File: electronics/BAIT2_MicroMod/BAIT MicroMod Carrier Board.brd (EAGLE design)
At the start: 95.2 x 96.5 mm, 110 parts, among them J1 microSD, J4 JST_6_PIN_VERTICAL, J5 QWIIC_RIGHT_ANGLE, U3 3.3V, U4 3.3V, U5 BQ27441-G1, X1 2.1mm DC, X2 BQ24074

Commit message: Board layout updates
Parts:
- removed ANT1: DIP SMA-K, Connector-new:SMA5P-SMD-5.1-6.5X6.5X16.5MM
- removed R16: DNP, Discrete-new:R0402
- moved R15 147.8 mm to (79.9, 78.2), turned to 90 degrees
- moved R14 147.5 mm to (82.0, 74.3), turned to 90 degrees
- moved TP2 139.2 mm to (69.8, 58.4)
- moved C12 138.2 mm to (80.0, 74.9)
- moved C11 135.1 mm to (80.0, 73.7)
- moved C10 132.0 mm to (72.4, 57.1), turned to 90 degrees
- moved ANT2 25.9 mm to (83.8, 78.7)
- moved LORA-E5 14.0 mm to (77.5, 64.8), turned to 90 degrees
- moved D_ASC 8.89 mm to (78.7, 47.0)
- moved D_RSSI\ 8.89 mm to (74.9, 47.0)
- moved D_RX 8.89 mm to (71.1, 47.0)
- moved D_TX 8.89 mm to (67.3, 47.0)
- moved E5_SWO 8.89 mm to (61.0, 63.5)
- moved MM_SWO 8.89 mm to (48.3, 50.8)
- moved R_ASC 8.89 mm to (78.7, 50.8)
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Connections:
- removed net N$10: ANT2.D, R16.2
- removed net N$13: ANT1.ANT, R15.2
- new net N$7: ANT2.D, R15.2
- net GND: no longer ANT1.GND1, ANT1.GND2, ANT1.GND3, ANT1.GND4
- net N$28: no longer R16.1
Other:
- board size 95.2 x 96.5 mm -> 95.2 x 94 mm
- board text added: "LiPo"

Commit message: Files for First Prototype production
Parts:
- removed 3V3_LED2: (no value), SparkFun-Jumpers:SMT-JUMPER_2_NC_TRACE_SILK
- removed BATT2: JST 2PH, adafruit:JST-PH-2-SMT-RA
- removed BT3: ML414H, SparkFun-Batteries:ML414H_IV01E
- removed D_ASC, D_RSSI\, D_RX: GREEN, SparkFun-LED:LED-0603
- removed D_TX: RED, SparkFun-LED:LED-0603
- removed LORA-E5: LoRa-E5-HF, moudle-new:MOUDLE28P-1.25-12X12X2.5MM
- removed MICROMOD: MICROMOD-2222-C, SparkFun-MicroMod:M.2-CONNECTOR-E
- removed REG1: S-1172B33-E6T1U, Ablic:HSOP-6_FH006-A-P-SD-2.1_ABL
- removed R_ASC: 4.7k, SparkFun-Resistors:0603
- removed R_RSSI, R_RX, R_TX: 1k, SparkFun-Resistors:0603
- removed S1: Reset, SparkFun-Switches:TACTILE_SWITCH_SMD_5.2MM
- removed S2: BOOT, SparkFun-Switches:TACTILE_SWITCH_SMD_5.2MM
- removed SOLAR_JST1: (no value), SparkFun-Connectors:JST-2-SMD
- removed U$23: (no value), microbuilder:ADAFRUIT_5MM
- removed USBC: (no value), SparkFun-Connectors:USB-C-16P-2LAYER-PADS
- removed X1: 2.1mm DC, microbuilder:DCJACK_2MM_SMT
- removed X2: BQ24074, adafruit_power:QFN16_3MM
- removed XBEE: XBEE, adafruit:XBEE
- added 3V3_LED, GND_CON: (no value), SparkFun-Jumpers:SMT-JUMPER_2_NC_TRACE_SILK
- added ANT1: 0868AT43A0020EANT_0868AT43A0020E_JOT, 2023-01-04_20-35-52_Library:ANT_0868AT43A0020E_JOT
- added BT1: ML414H, SparkFun-Batteries:ML414H_IV01E
- added C1, C17, C19, C20, C21, C23, C31, C8: 2.2uF, SparkFun-Capacitors:0603-POLAR
- added C16, C2, C24, C9: 0.1uF, SparkFun-Capacitors:EIA3216
- added C18: 0.15uF, SparkFun-Capacitors:EIA3216
- added C32, C34, C35, C37, C38: 100nf, OPL_Capacitor:C0603
- added C33: 4.7uF, Discrete-new:C0603
- added C36: 10uf, OPL_Capacitor:AVX-A
- added C39: 220pF, Capacitor:CAPC1608X85
- added D2, D3, D4: GREEN, SparkFun-LED:LED-0603
- added D5: RED, SparkFun-LED:LED-0603
- added F1: 6V/2A, Circuit-Protection:FUSC3215X82N
- added FB1: 600Ω/1.8A, SparkFun-Coils:0603
- added J10: QWIIC_RIGHT_ANGLE, SM04B-SRSS-TB_LF__SN_:JST_SM04B-SRSS-TB(LF)(SN)
- added J15: SM06B-SRSS-TB(LF)(SN), SM06B-SRSS-TB_LF__SN_:JST_SM06B-SRSS-TB(LF)(SN)
- added J2: ST-TF-003A, ST-TF-003A:SUNTECH_ST-TF-003A
- added J3: (no value), SparkFun-RF:XBEE-SMD
- added J6: JST 2PH, adafruit:JST-PH-2-SMT-RA
- added J7: MICROMOD-2222-C, SparkFun-MicroMod:M.2-CONNECTOR-E
- added J8: (no value), SparkFun-Connectors:JST-2-SMD
- added J9: (no value), SparkFun-Connectors:USB-C-16P-2LAYER-PADS
- added LINEIN, LINEOUT: (no value), SparkFun-Connectors:1X03
- added MIC_3V3, MIC_GND: (no value), SparkFun-Jumpers:SMT-JUMPER_3_2-NC_TRACE_SILK
- added MK1: ICS-43432, Audio-Devices:ICS-43432
- added MK1_LR: MK1_LR, SparkFun-Jumpers:SMT-JUMPER_3_1-NC_TRACE_SILK
- added MK2: SPH0645LM4H-B, SPH0645LM4H-B:MIC_SPH0645LM4H-B
- added MK2_LR: MK2_LR, SparkFun-Jumpers:SMT-JUMPER_3_1-NC_TRACE_SILK
- added R11, R5: 4.7K, OPL_Resistor:R0603
- added R18: 100K, OPL_Resistor:R0603
- added R2: 2.2K, OPL_Resistor:R0603
- added R4: 0R, OPL_Resistor:R0603
- added R6, R7, R8: 1K 1/10W, OPL_Resistor:R0603
- added SW1, SW2: SKQGADE010, OPL_Switch:SW4-SMD-5.2X5.2X1.5MM
- added TP1, TP3: PTR1TP06R, testpad:TP06R
- added U1: SGTL5000-32, Freescale:QFN-32-5MM
- added U10: TSL25911, 2023-02-07_20-42-29_Library:SON-06-FN_2000X2400_AMS
- added U2: AP7313, 2022-08-05_10-01-44_Library:SOT-23_DIO
- added U6: BQ24074, adafruit_power:QFN16_3MM
- added U7: LoRa-E5-HF, moudle-new:MOUDLE28P-1.25-12X12X2.5MM
- added U8: S-1172B33-E6T1U, Ablic:HSOP-6_FH006-A-P-SD-2.1_ABL
- added U9: BOSCH_TOOLS_BME680BOSCH_TOOLS_BME680_0_0, Bosch Tools - BME680:BOSCH_TOOLS_BME680_0
- C10: value 4.7uF -> 4.7uf; device Discrete-new:C0603 -> OPL_Capacitor:C0603
- C13, C14, C28: value 1.0uF -> 1uf; device SparkFun-Capacitors:0603 -> OPL_Capacitor:C0603
- C15, C22, C4, C5: value 10uF -> 4.7uf; device microbuilder:0805-NO -> OPL_Capacitor:C0603
- C25, C30: value 0.22uF -> 220nf; device SparkFun-Capacitors:0603 -> OPL_Capacitor:C0603
- C26, C29, C6: value 0.1uF -> 100nf; device SparkFun-Capacitors:0603 -> OPL_Capacitor:C0603
- C27: value 10uF -> 10uf; device SparkFun-Capacitors:EIA3216 -> OPL_Capacitor:AVX-A
- C3: value 1.0uF -> 1uf; device SparkFun-Capacitors:0603-CAP -> OPL_Capacitor:C0603
- D17, D21: device microbuilder:CHIPLED_0603 -> SparkFun-LED:LED-0603
- J1: value microSD -> SJ-43516-SMT; device SparkFun-Connectors:MICRO-SD-SOCKET -> SnapEDA-Library:CUI_SJ-43516-SMT
- R1: value 180 -> 200K; device SparkFun-Resistors:0603 -> OPL_Resistor:R0603
- R10: value 20k -> 20K; device SparkFun-Resistors:0603 -> OPL_Resistor:R0603
- R14, R15: device Discrete-new:R0402 -> OPL_Resistor:R0603
- R21, R3, R36: value 100k -> 100K; device SparkFun-Resistors:0603 -> OPL_Resistor:R0603
- R23: value 1k -> 1K 1/10W; device SparkFun-Resistors:0603 -> OPL_Resistor:R0603
- R24: value 4.7k -> 4.7K; device SparkFun-Resistors:0603 -> OPL_Resistor:R0603
- R32: value 3.3k -> 3.3K; device SparkFun-Resistors:0603 -> OPL_Resistor:R0603
- R34, R35: value 2.2k -> 2.2K; device SparkFun-Resistors:0603 -> OPL_Resistor:R0603
- R38, R41, R42, R43, R44: value 10K -> 10K 1/10W; device microbuilder:0603-NO -> OPL_Resistor:R0603
- R39: device microbuilder:0603-NO -> OPL_Resistor:R0603
- R40: value 1K -> 1K 1/10W; device microbuilder:0603-NO -> OPL_Resistor:R0603
- R9: value 10k -> 10K 1/10W; device SparkFun-Resistors:0603 -> OPL_Resistor:R0603
- TH1, TH2, TH3, TH4: device varistor:CT/CN0603 -> NTCG163JX103DT1S:THERM_NTCG163JX103DT1S
- moved POWER_PINS 93.0 mm to (81.3, 3.81)
- moved J4 86.3 mm to (14.6, 50.5), turned to 180 degrees
- moved R14 68.2 mm to (13.9, 71.8), turned to 270 degrees
- moved C12 67.5 mm to (12.6, 70.4)
- moved ANT2 67.3 mm to (16.5, 77.5), turned to 90 degrees
- moved C11 64.9 mm to (15.2, 70.3), turned to 180 degrees
- moved R15 64.3 mm to (15.7, 74.0)
- moved R34 55.8 mm to (36.8, 36.8), turned to 0 degrees
- moved C14 54.5 mm to (32.6, 30.5), turned to 180 degrees
- moved R21 54.5 mm to (34.3, 33.0), turned to 270 degrees
- moved J5 51.7 mm to (40.6, 41.9), turned to 270 degrees
- moved R35 51.3 mm to (39.1, 36.8), turned to 0 degrees
- moved U4 51.2 mm to (35.6, 30.5), turned to 90 degrees
- moved C13 49.7 mm to (42.4, 43.2), turned to 180 degrees
- moved QWIIC_PWR 48.4 mm to (43.2, 36.8)
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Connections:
- removed net GND1: SOLAR_JST1.1, X1.2, X1.3
- removed net OUT: X2.5
- removed net PA15/SDA: LORA-E5.6
- removed net PB15/SCL: LORA-E5.5
- removed net RX2: MICROMOD.20
- removed net THERM: TH1.1, TH3.1, THERM2.2, X2.1
- removed net TX2: MICROMOD.22
- removed net V+1: REG1.6
- removed net VCC: XBEE.1
- new net 3V3_B: C34.1, C35.1, J10.2, J15.1, MIC_3V3.2, MK1_LR.1, MK2_LR.3, TP1.TP, U10.5, U9.8
- new net 3V3_ICS: C37.1, MIC_3V3.3, MK1.3
- new net 3V3_SPH: C38.1, C39.1, MIC_3V3.1, MK2.5
- new net AGND: C18.-, GND_CON.1, LINEIN.1, LINEOUT.1, U1.1, U1.3, U1.7
- new net GND_B: C32.2, C34.2, C35.2, J10.1, J10.S1, J10.S2, J15.2, J15.S1, J15.S2, MIC_GND.2, MK1_LR.3, MK2_LR.1, R18.1, TP3.TP, U10.3, U9.1, U9.5, U9.7
- new net GND_ICS: C37.2, MIC_GND.3, MK1.2, MK1.4
- new net GND_SPH: C38.2, C39.2, MIC_GND.1, MK2.3
- new net INT_B: U10.2
- new net N$11: ANT1.1, R4.2
- new net N$13: C19.-, LINEOUT.3
- new net N$14: C20.-, LINEOUT.2
- new net N$15: C21.-, LINEIN.3
- new net N$17: C23.-, LINEIN.2
- new net N$18: C19.+, U1.11
- new net N$20: C20.+, U1.12
- new net N$21: C21.+, U1.13
- new net N$22: C23.+, U1.14
- new net N$33: C24.-, J1.1, R2.2
- new net N$35: J1.3, U1.2
- new net N$36: F1.1, J9.VBUS1, J9.VBUS2
- new net N$38: C18.+, U1.10
- new net N$39: C31.+, R2.1, U1.16
- new net N$40: C24.+, U1.15
- new net N$41: C8.+, U1.30, U2.2
- new net N$46: C1.+, C2.+, FB1.2, U1.5
- new net N$54: C32.1, R11.2, U9.6
- new net N$55: R11.1, U9.2
- new net N$8: J1.2, U1.6
- new net SCK_B: J15.3, MK1.6, MK2.4
- new net SCL_B: J10.4, U10.1, U9.4
- new net SDA_B: J10.3, U10.6, U9.3
- new net SD_B: J15.4, MK1.7, MK2.6, R18.2
- new net SEL_MK1: MK1.1, MK1_LR.2
- new net SEL_MK2: MK2.2, MK2_LR.2
- new net USB_VIN: D15.A, F1.2, J7.9
- new net WS_B: J15.5, MK1.5, MK2.1
- net !BOOT!: now also J7.11, SW2.2; no longer MICROMOD.11, S2.3, S2.4
- net !CE: now also U6.4; no longer X2.4
- net !CHG: now also U6.9; no longer X2.9
- net !PGOOD: now also U6.7; no longer X2.7
- net !RESET!: now also J7.6, SW1.2; no longer MICROMOD.6, S1.3, S1.4
- net 3.3V: now also 3V3_LED.2, C16.+, C17.+, C33.2, C36.+, C9.+, FB1.1, J3.1, J7.2, J7.74, J_RX.1, U1.20, U2.1, U7.1; no longer 3V3_LED2.2, J_RX.2, LORA-E5.1, MICROMOD.2, MICROMOD.74
- net 3.3V_EN: now also J7.4; no longer MICROMOD.4
- net 3.3V_LP: now also J2.4; no longer J1.VCC
- net A0: now also J7.34; no longer MICROMOD.34
- net A1: now also J7.38; no longer MICROMOD.38
- net ASC: now also J3.15; no longer XBEE.15
- net CLK/SCK: now also J2.5, JP_SCK.2; no longer J1.SCLK, JP_SCK.3
- net CMD/CIPO: now also J2.3, JP_CIPO.2; no longer J1.DI/CMD, JP_CIPO.3
- net D0: now also J7.10; no longer MICROMOD.10
- net D1: now also J7.18; no longer MICROMOD.18
- net DAT0/COPI: now also J2.7, JP_COPI.2; no longer J1.DO/DAT0, JP_COPI.3
- net DAT3/!CS!: now also J2.2, JP_CS.2; no longer J1.CS/DAT3, JP_CS.3
- net GND: now also BT1.-, C1.-, C16.-, C17.-, C2.-, C31.-, C33.1, C36.-, C8.-, C9.-, D2.C, D3.C, GND_CON.2, J2.6, J2.G1, J2.G2, J2.G3, J2.G4, J3.10, J6.2, J7.1, J7.33, J7.36, J7.39, J7.45, J7.7, J7.75, J8.1, J9.GND, J9.GND2, SW1.4, SW2.4, U1.31, U1.32, U1.PAD, U2.3, U6.14, U6.6, U6.8, U6.THERMAL, U7.14, U7.16, U7.2, U7.22, U8.2, U8.5; no longer BATT2.2, BT3.-, D_ASC.C, D_RSSI\.C, J1.CD1, J1.GND, J1.GND1, J1.GND3, LORA-E5.14, LORA-E5.16, LORA-E5.2, LORA-E5.22, MICROMOD.1, MICROMOD.33, MICROMOD.36, MICROMOD.39, MICROMOD.45, MICROMOD.7, MICROMOD.75, REG1.2, REG1.5, S1.1, S1.2, S2.1, S2.2, USBC.GND, USBC.GND2, X2.14, X2.6, X2.8, X2.THERMAL, XBEE.10
- net GPOUT: now also J7.71
- net HEADER_!CS!: now also J7.40; no longer MICROMOD.40
- net I2C_!INT!: now also J7.16; no longer MICROMOD.16
- net I2C_SCL: now also J7.14, U1.29; no longer MICROMOD.14
- net I2C_SDA: now also J7.12, U1.27; no longer MICROMOD.12
- net I2S_SCK: now also J7.50; no longer MICROMOD.50
- net I2S_SD: now also J7.54; no longer MICROMOD.54
- net I2S_WS: now also J7.52; no longer MICROMOD.52
- net ILIM: now also U6.12; no longer X2.12
- net ISET: now also U6.16; no longer X2.16
- net ITERM: now also U6.15; no longer X2.15
- net LR_SEL: now also J7.73; no longer MICROMOD.73
- net N$16: now also 3V3_LED.1; no longer 3V3_LED2.1
- net N$19: now also U7.28; no longer LORA-E5.28
- net N$23: now also BT1.+; no longer BT3.+
- net N$25: now also R5.2; no longer R_ASC.2
- net N$28: now also R4.1
- net N$3: now also J_RX.2, R7.2; no longer J_RX.1, R_RX.2
- net N$30: now also J8.2; no longer SOLAR_JST1.2, X1.1, X1.1'
- net N$34: now also D2.A, R5.1; no longer D_ASC.A, R_ASC.1
- net N$4: now also J9.A5; no longer USBC.A5
- net N$42: now also R6.2; no longer R_RSSI.2
- net N$43: now also D3.A, R6.1; no longer D_RSSI\.A, R_RSSI.1
- net N$44: now also R8.2; no longer R_TX.2
- net N$45: now also D5.A, R8.1; no longer D_TX.A, R_TX.1
- net N$48: now also J1.4, U1.4; no longer D15.A, USBC.VBUS1, USBC.VBUS2
- net N$5: now also J9.B5; no longer USBC.B5
- net N$6: now also U8.1; no longer REG1.1
- net N$9: now also D4.A, R7.1; no longer D_RX.A, R_RX.1
- net PA0/D0: now also U7.23; no longer LORA-E5.23
- net PA10/MOSI: now also U7.27; no longer LORA-E5.27
- net PA13/SWDIO: now also U7.3; no longer LORA-E5.3
- net PA14/SWCLK: now also U7.4; no longer LORA-E5.4
- net PA2/TX2: now also U7.19; no longer LORA-E5.19
- net PA3/RX2: now also E5_EXTRA_PINS.14, U7.18; no longer E5_EXTRA_PINS.12, LORA-E5.18
- net PA9/D9: now also E5_EXTRA_PINS.11, U7.21; no longer E5_EXTRA_PINS.15, LORA-E5.21
- net PB10/D10: now also E5_EXTRA_PINS.12, U7.20; no longer E5_EXTRA_PINS.14, LORA-E5.20
- net PB13/BOOT/SCK: now also U7.24; no longer LORA-E5.24
- net PB14/MISO: now also U7.26; no longer LORA-E5.26
- net PB3/A3: now also U7.8; no longer LORA-E5.8
- net PB4/A4: now also U7.7; no longer LORA-E5.7
- net PB5/LED: now also E5_EXTRA_PINS.10, U7.11; no longer E5_EXTRA_PINS.8, LORA-E5.11
- net PB9/NSS: now also U7.25; no longer LORA-E5.25
- net PC0/RX1: now also E5_EXTRA_PINS.8, U7.13; no longer E5_EXTRA_PINS.10, LORA-E5.13
- net PC1/TX1: now also U7.12; no longer LORA-E5.12
- net PERIPHERAL_PWR_CTRL: now also J7.42; no longer MICROMOD.42
- net PWM0: now also J7.32; no longer MICROMOD.32
- net PWM1: now also J7.47; no longer MICROMOD.47
- net QWIIC_PWR_CTRL: now also J7.44; no longer MICROMOD.44
- net RF: now also U7.15; no longer LORA-E5.15
- net RSSI: now also J3.6; no longer XBEE.6
- net RST: now also E5_EXTRA_PINS.15, U7.17; no longer E5_EXTRA_PINS.11, LORA-E5.17
- net RTC_3V: now also J7.72; no longer MICROMOD.72
- net RX: now also D4.C, J3.2, J7.19, U7.9; no longer D_RX.C, LORA-E5.9, MICROMOD.19, XBEE.2
- net SD_!CS!: now also J7.55; no longer MICROMOD.55
- net SD_CLK: now also J7.60, JP_SCK.3; no longer JP_SCK.2, MICROMOD.60
- net SD_CMD: now also J7.62, JP_CIPO.3; no longer JP_CIPO.2, MICROMOD.62
- net SD_DATA0: now also J7.64, JP_COPI.3; no longer JP_COPI.2, MICROMOD.64
- net SD_DATA1: now also J2.8, J7.66; no longer J1.DAT1, MICROMOD.66
- net SD_DATA2: now also J2.1, J7.68; no longer J1.DAT2, MICROMOD.68
- net SD_DATA3: now also J7.70, JP_CS.3; no longer JP_CS.2, MICROMOD.70
- net SPI_CIPO: now also J7.61; no longer MICROMOD.61
- net SPI_COPI: now also J7.59; no longer MICROMOD.59
- net SPI_SCK: now also J7.57; no longer MICROMOD.57
- net SWDCK: now also J7.21; no longer MICROMOD.21
- net SWDIO: now also J7.23; no longer MICROMOD.23
- net TS: now also TH1.1, TH3.1, THERM2.2, U6.1
- net TX: now also D5.C, J3.3, J7.17, U7.10; no longer D_TX.C, LORA-E5.10, MICROMOD.17, XBEE.3
- net USB_D+: now also J7.3, J9.A6, J9.B6; no longer MICROMOD.3, USBC.A6, USBC.B6
- net USB_D-: now also J7.5, J9.A7, J9.B7; no longer MICROMOD.5, USBC.A7, USBC.B7
- net V+: now also U6.10, U6.11, U6.5, U8.6; no longer X2.10, X2.11
- net VBUS: now also U6.13; no longer X2.13
- net VIN: now also J6.1; no longer BATT2.1, MICROMOD.9
- net VIN/3: now also J7.49; no longer MICROMOD.49
- net V_BATT: now also U6.2, U6.3; no longer X2.2, X2.3
- net XB_ON: now also J3.13; no longer XBEE.13
- net XB_RST: now also J3.5; no longer XBEE.5
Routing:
- net 3.3V: track 0.00 -> 271.8 mm, vias 0 -> 13
- net GND: track 7.68 -> 153.4 mm, vias 1 -> 17
- net V+: track 10.4 -> 109.5 mm, vias 1 -> 5
- net VBUS: track 13.9 -> 101.7 mm, vias 0 -> 3
- net !RESET!: track 0.00 -> 79.7 mm, vias 0 -> 2
- net TS: track 0.00 -> 74.5 mm, vias 0 -> 4
- net I2C_SCL: track 0.00 -> 74.4 mm, vias 0 -> 4
- net I2C_SDA: track 0.00 -> 74.1 mm, vias 0 -> 2
- net !BOOT!: track 0.00 -> 72.1 mm, vias 0 -> 2
- net USB_VIN: track 0.00 -> 69.8 mm, vias 0 -> 2
- net RF: track 0.00 -> 66.0 mm, vias 0 -> 2
- net RX: track 0.00 -> 66.0 mm, vias 0 -> 4
- net RST: track 0.00 -> 63.7 mm, vias 0 -> 3
- net USB_D+: track 0.00 -> 61.5 mm, vias 0 -> 6
- net TX: track 0.00 -> 61.0 mm, vias 0 -> 4
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- added copper zone on layer 1, net CUTOUT
- added copper zone on layer 1, net GND
- added copper zone on layer 16, net GND_B
- removed copper zone on layer 1, net OUT
- removed copper zone on layer 1, net VLIPO
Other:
- board size 95.2 x 94 mm -> 92.7 x 80 mm
- board text added: "50 ohm impedance control on the RF line from its origin on the WIO-E5 chip through to ANT1 and ANT2"
- board text added: "BAIT"
- board text added: "SmallThings"
- board text added: "V2.0.1 (23F14)"
- board text added: "by"
- board text removed: "0.5A"
- board text removed: "1.0A"
- board text removed: "1.5A"
- board text removed: "LiPo"
- board text removed: "LiPo Batt"
- board text removed: "Solar/DC In is 10V Max"
- board text removed: "Use any 3.7/4.2V LiPoly/LiIon"

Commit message: Schematic fix for faulty connection between Teensy and LORA-E5
Swapped RX and TX pins. Fixes #7
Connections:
- net RX: now also U7.10; no longer U7.9
- net TX: now also U7.9; no longer U7.10
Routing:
- net TX: track 61.0 -> 56.5 mm
- net RX: track 66.0 -> 61.8 mm
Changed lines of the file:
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@@
 <wire x1="42.4197125" y1="52.9932" x2="42.7665125" y2="53.34" width="0.2032" layer="1"/>
 <wire x1="42.7665125" y1="53.34" x2="45.157125" y2="53.34" width="0.2032" layer="1"/>
-<wire x1="62.25" y1="59.19631875" x2="62.25" y2="60.04" width="0.2032" layer="1"/>
-<wire x1="60.20368125" y1="57.15" x2="62.25" y2="59.19631875" width="0.2032" layer="1"/>
 <wire x1="45.157125" y1="53.34" x2="48.967125" y2="57.15" width="0.2032" layer="1"/>
 <wire x1="48.967125" y1="57.15" x2="51.816" y2="57.15" width="0.2032" layer="1"/>
@@
 <contactref element="J3" pad="3"/>
 <contactref element="J7" pad="17"/>
-<contactref element="U7" pad="10"/>
-<wire x1="62.25" y1="60.04" x2="62.25" y2="58.44" width="0.2032" layer="1"/>
 <wire x1="62.25" y1="58.44" x2="62.23" y2="58.42" width="0.2032" layer="1"/>
 <via x="62.23" y="58.42" extent="1-16" drill="0.35"/>
@@
 <wire x1="62.23" y1="49.53" x2="61.353" y2="48.653" width="0.2032" layer="1"/>
 <wire x1="61.353" y1="48.653" x2="61.353" y2="48.26" width="0.2032" layer="1"/>
+<contactref element="U7" pad="9"/>
+<wire x1="61" y1="59.19631875" x2="61" y2="60.04" width="0.2032" layer="1"/>
+<wire x1="62.23" y1="58.42" x2="61" y2="59.19631875" width="0" layer="19" extent="1-1"/>
+<wire x1="60.20368125" y1="57.15" x2="61" y2="59.19631875" width="0" layer="19" extent="1-1"/>
 </signal>
 <signal name="RX" class="2">
@@
 <wire x1="42.2724125" y1="53.3488" x2="42.7636125" y2="53.84" width="0.2032" layer="1"/>
 <wire x1="42.7636125" y1="53.84" x2="44.95" y2="53.84" width="0.2032" layer="1"/>
-<wire x1="61" y1="59.19631875" x2="61" y2="60.04" width="0.2032" layer="1"/>
 <wire x1="44.95" y1="53.84" x2="48.76000625" y2="57.65000625" width="0.2032" layer="1"/>
 <wire x1="48.76000625" y1="57.65000625" x2="52.705" y2="57.65000625" width="0.2032" layer="1"/>
 <wire x1="52.705" y1="57.65000625" x2="59.4536875" y2="57.65000625" width="0.2032" layer="1"/>
-<wire x1="59.4536875" y1="57.65000625" x2="61" y2="59.19631875" width="0.2032" layer="1"/>
 <via x="53.9402" y="73.66" extent="1-16" drill="0.35"/>
 <wire x1="53.9402" y1="73.66" x2="52.7737" y2="72.4935" width="0.2032" layer="16"/>
@@
 <contactref element="J3" pad="2"/>
 <contactref element="J7" pad="19"/>
-<contactref element="U7" pad="9"/>
 <wire x1="65.163" y1="48.26" x2="64.77" y2="48.653" width="0.2032" layer="1"/>
 <wire x1="64.77" y1="48.653" x2="64.77" y2="49.53" width="0.2032" layer="1"/>
@@
 <wire x1="62.865" y1="51.435" x2="62.865" y2="61.6698" width="0.2032" layer="16"/>
 <via x="62.865" y="61.6698" extent="1-16" drill="0.35"/>
-<wire x1="61.546" y1="61.2952125" x2="61.546" y2="60.586" width="0.2032" layer="1"/>
-<wire x1="61.546" y1="60.586" x2="61" y2="60.04" width="0.2032" layer="1"/>
 <wire x1="62.865" y1="61.6698" x2="61.9205875" y2="61.6698" width="0.2032" layer="1"/>
-<wire x1="61.9205875" y1="61.6698" x2="61.546" y2="61.2952125" width="0.2032" layer="1"/>
 <wire x1="53.9402" y1="73.66" x2="54" y2="73.7198" width="0.2032" layer="1"/>
 <wire x1="54" y1="73.7198" x2="54" y2="75.15" width="0.2032" layer="1"/>
+<contactref element="U7" pad="10"/>
+<wire x1="62.25" y1="59.19631875" x2="62.25" y2="60.04" width="0.2032" layer="1"/>
+<wire x1="61.9205875" y1="61.6698" x2="62.25" y2="60.04" width="0" layer="19" extent="1-1"/>
+<wire x1="59.4536875" y1="57.65000625" x2="62.25" y2="59.19631875" width="0" layer="19" extent="1-1"/>
 </signal>
 <signal name="RTC_3V" class="1">

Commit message: Connect SGTL to I2S2 pins on micromod connector
Solves #6 in schematic, but creates #14
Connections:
- removed net D0: J7.10, MICROMOD_EXTRA_PINS.4
- removed net D1: J7.18, MICROMOD_EXTRA_PINS.3
- removed net PWM0: J7.32, R1.1
- removed net PWM1: J7.47, MICROMOD_EXTRA_PINS.5
- new net I2S2_MCLK: J7.63, U1.21
- new net I2S2_RX: J7.18, U1.25
- new net I2S2_SCK: J7.10, U1.24
- new net I2S2_TX: J7.47, U1.26
- new net I2S2_WS: J7.32, U1.23
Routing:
- net D0: track 48.3 -> 0.00 mm
- net D1: track 47.3 -> 0.00 mm
- net PWM1: track 46.7 -> 0.00 mm
- net PWM0: track 43.9 -> 0.00 mm, vias 4 -> 0
- net I2S2_WS: track 0.00 -> 42.1 mm, vias 0 -> 4
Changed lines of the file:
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@@
 <wire x1="4.826" y1="65.405" x2="1.778" y2="62.357" width="0.2032" layer="16"/>
 </signal>
-<signal name="PWM0">
-<contactref element="R1" pad="1"/>
+<signal name="I2S2_WS">
 <wire x1="33.25" y1="56.885" x2="33.25" y2="55.6302" width="0.2032" layer="1"/>
 <via x="33.25" y="55.6302" extent="1-16" drill="0.35"/>
@@
 <wire x1="52.2078" y1="38.0891625" x2="58.48348125" y2="31.81348125" width="0.2032" layer="16"/>
 <via x="58.48348125" y="31.81348125" extent="1-16" drill="0.35"/>
-<wire x1="58.48348125" y1="31.81348125" x2="58.48348125" y2="30.12348125" width="0.2032" layer="1"/>
-<wire x1="58.48348125" y1="30.12348125" x2="58.42" y2="29.972" width="0.2032" layer="1"/>
 <contactref element="J7" pad="32"/>
-</signal>
-<signal name="PWM1">
-<contactref element="MICROMOD_EXTRA_PINS" pad="5"/>
-<contactref element="J7" pad="47"/>
-<wire x1="12.7" y1="46.99" x2="27.94" y2="46.99" width="0.2032" layer="1"/>
-<wire x1="28.43808125" y1="45.66969375" x2="28.77865625" y2="45.32911875" width="0.2032" layer="1"/>
-<wire x1="28.77865625" y1="45.32911875" x2="29.26030625" y2="45.32911875" width="0.2032" layer="1"/>
-<wire x1="29.26030625" y1="45.32911875" x2="29.60088125" y2="45.66969375" width="0.2032" layer="1"/>
-<wire x1="29.60088125" y1="45.66969375" x2="29.60088125" y2="46.15134375" width="0.2032" layer="1"/>
-<wire x1="29.60088125" y1="46.15134375" x2="29.5" y2="46.252225" width="0.2032" layer="1"/>
-<wire x1="29.5" y1="46.252225" x2="29.5" y2="49.335" width="0.2032" layer="1"/>
-<wire x1="27.94" y1="46.99" x2="28.43808125" y2="46.49191875" width="0.2032" layer="1"/>
-<wire x1="28.43808125" y1="46.49191875" x2="28.43808125" y2="45.66969375" width="0.2032" layer="1"/>
-<wire x1="0.5842" y1="49.16250625" x2="1.28350625" y2="48.4632" width="0.2032" layer="1"/>
-<wire x1="1.28350625" y1="48.4632" x2="2.27249375" y2="48.4632" width="0.2032" layer="1"/>
-<wire x1="1.778" y1="59.817" x2="1.778" y2="58.96529375" width="0.2032" layer="1"/>
-<wire x1="1.778" y1="58.96529375" x2="0.5842" y2="57.77149375" width="0.2032" layer="1"/>
-<wire x1="2.97829375" y1="49.169" x2="10.521" y2="49.169" width="0.2032" layer="1"/>
-<wire x1="10.521" y1="49.169" x2="12.7" y2="46.99" width="0.2032" layer="1"/>
-<wire x1="2.27249375" y1="48.4632" x2="2.97829375" y2="49.169" width="0.2032" layer="1"/>
-<wire x1="0.5842" y1="57.77149375" x2="0.5842" y2="49.16250625" width="0.2032" layer="1"/>
-</signal>
-<signal name="D0">
-<contactref element="MICROMOD_EXTRA_PINS" pad="4"/>
-<wire x1="38.75" y1="56.885" x2="38.75" y2="58.1398" width="0.2032" layer="1"/>
-<contactref element="J7" pad="10"/>
-<wire x1="38.75" y1="58.1398" x2="30.04518125" y2="66.84461875" width="0.2032" layer="1"/>
-<wire x1="30.04518125" y1="66.84461875" x2="7.15461875" y2="66.84461875" width="0.2032" layer="1"/>
-<wire x1="7.15461875" y1="66.84461875" x2="3.81" y2="63.5" width="0.2032" layer="1"/>
-<wire x1="3.81" y1="63.5" x2="3.81" y2="59.309" width="0.2032" layer="1"/>
-<wire x1="3.81" y1="59.309" x2="1.778" y2="57.277" width="0.2032" layer="1"/>
-</signal>
-<signal name="D1">
-<contactref element="MICROMOD_EXTRA_PINS" pad="3"/>
-<contactref element="J7" pad="18"/>
-<wire x1="4.445" y1="57.404" x2="1.778" y2="54.737" width="0.2032" layer="1"/>
-<wire x1="36.75" y1="56.885" x2="36.654" y2="56.981" width="0.2032" layer="1"/>
-<wire x1="36.654" y1="56.981" x2="36.654" y2="58.058025" width="0.2032" layer="1"/>
-<wire x1="36.654" y1="58.058025" x2="28.672025" y2="66.04" width="0.2032" layer="1"/>
-<wire x1="4.445" y1="62.865" x2="4.445" y2="57.404" width="0.2032" layer="1"/>
-<wire x1="28.672025" y1="66.04" x2="7.62" y2="66.04" width="0.2032" layer="1"/>
-<wire x1="7.62" y1="66.04" x2="4.445" y2="62.865" width="0.2032" layer="1"/>
+<contactref element="U1" pad="23"/>
+<wire x1="24.11" y1="34.58" x2="33.25" y2="55.6302" width="0" layer="19" extent="1-1"/>
 </signal>
 <signal name="SPI_COPI" class="2">
@@
 <via x="83.83" y="7.03" extent="1-16" drill="0.3048"/>
 </signal>
+<signal name="I2S2_TX">
+<contactref element="J7" pad="47"/>
+<contactref element="U1" pad="26"/>
+<wire x1="25.11" y1="35.58" x2="29.5" y2="49.335" width="0" layer="19" extent="1-1"/>
+</signal>
+<signal name="I2S2_SCK">
+<contactref element="J7" pad="10"/>
+<contactref element="U1" pad="24"/>
+<wire x1="24.61" y1="34.53" x2="38.75" y2="56.885" width="0" layer="19" extent="1-1"/>
+</signal>
+<signal name="I2S2_RX">
+<contactref element="J7" pad="18"/>
+<contactref element="U1" pad="25"/>
+<wire x1="25.16" y1="35.08" x2="36.75" y2="56.885" width="0" layer="19" extent="1-1"/>
+</signal>
+<signal name="I2S2_MCLK">
+<contactref element="J7" pad="63"/>
+<contactref element="U1" pad="21"/>
+<wire x1="23.11" y1="34.58" x2="25.5" y2="49.335" width="0" layer="19" extent="1-1"/>
+</signal>
 </signals>

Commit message: Fixes enable issue with main 3.3V regulator
Resolves #3 in schematic and board
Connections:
- net V+: now also U8.3
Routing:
- net V+: track 109.5 -> 113.7 mm
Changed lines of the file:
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@@
 <wire x1="39.37" y1="30.48" x2="39.5" y2="30.35" width="0.2032" layer="1"/>
 <wire x1="48.9" y1="30.3276" x2="48.9" y2="31.11" width="0.2032" layer="1"/>
+<contactref element="U8" pad="3"/>
+<wire x1="45.08" y1="35.7124" x2="45.08" y2="34.158" width="0.508" layer="1"/>
+<wire x1="45.08" y1="34.158" x2="43.18" y2="32.258" width="0.508" layer="1"/>
 </signal>
 <signal name="1.8V" class="1">

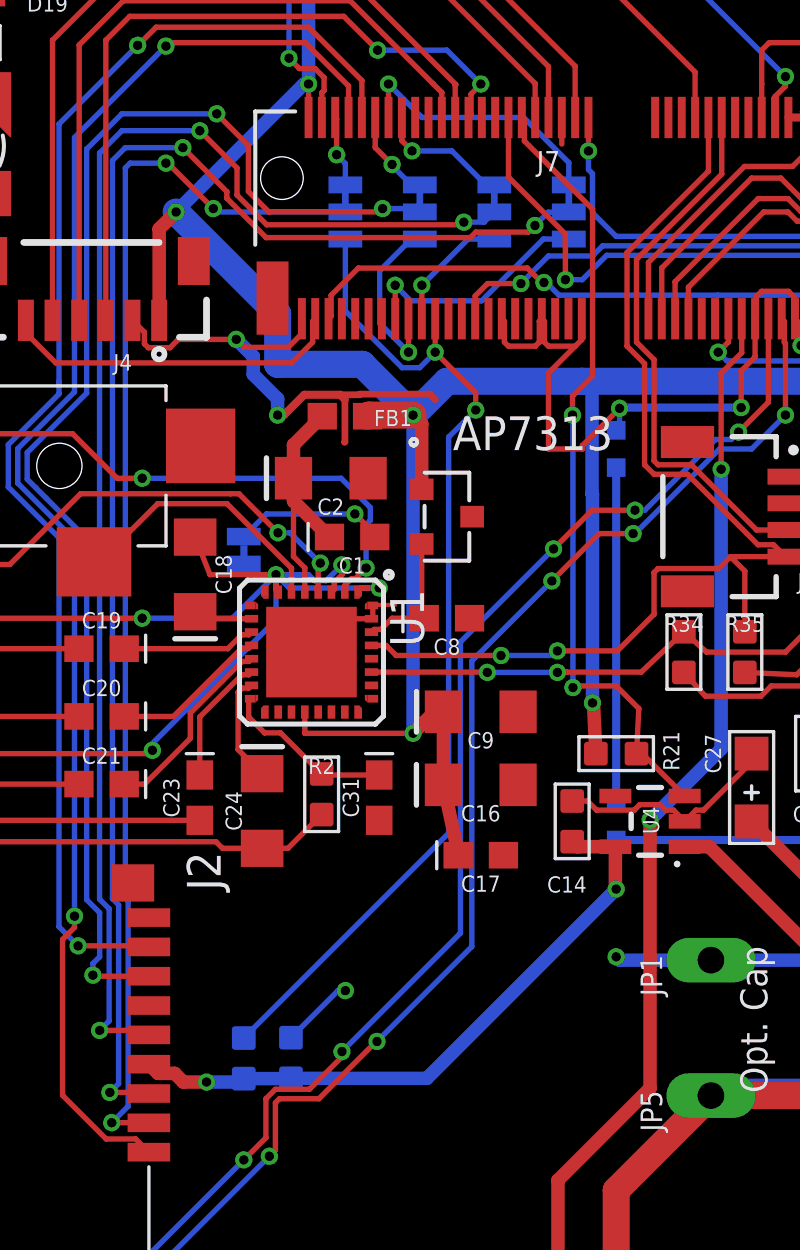
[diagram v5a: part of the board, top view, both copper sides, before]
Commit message: Removes secondary options for connecting to SD card
Resolves #22
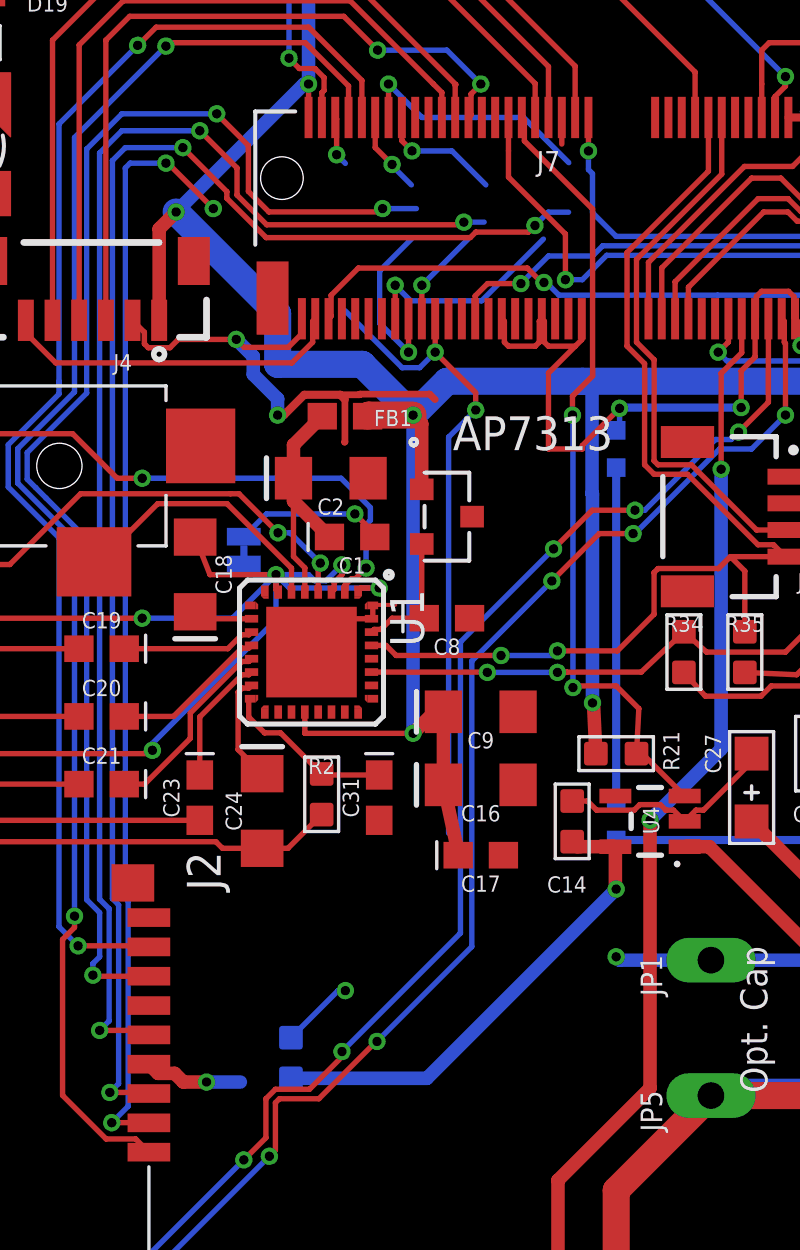
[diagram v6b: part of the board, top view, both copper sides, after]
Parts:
- removed JP_CIPO, JP_COPI, JP_CS, JP_SCK: (no value), SparkFun-Jumpers:SMT-JUMPER_3_1-NC_TRACE_SILK
- removed R3: 100K, OPL_Resistor:R0603
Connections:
- removed net CLK/SCK: J2.5, JP_SCK.2
- removed net CMD/CIPO: J2.3, JP_CIPO.2
- removed net DAT0/COPI: J2.7, JP_COPI.2
- removed net DAT3/!CS!: J2.2, JP_CS.2
- net 3.3V_LP: no longer R3.2
- net SD_!CS!: no longer JP_CS.1, R3.1
- net SD_CLK: now also J2.5; no longer JP_SCK.3
- net SD_CMD: now also J2.3; no longer JP_CIPO.3
- net SD_DATA0: now also J2.7; no longer JP_COPI.3
- net SD_DATA3: now also J2.2; no longer JP_CS.3
- net SPI_CIPO: no longer JP_CIPO.1
- net SPI_COPI: no longer JP_COPI.1
- net SPI_SCK: no longer JP_SCK.1
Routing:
- net CMD/CIPO: track 55.9 -> 0.00 mm, vias 3 -> 0
- net SD_CMD: track 10.1 -> 65.2 mm, vias 1 -> 4
- net CLK/SCK: track 52.5 -> 0.00 mm, vias 3 -> 0
- net SD_CLK: track 5.03 -> 56.7 mm, vias 1 -> 4
- net DAT0/COPI: track 50.9 -> 0.00 mm, vias 3 -> 0
- net SD_DATA0: track 3.41 -> 53.9 mm, vias 1 -> 4
- net DAT3/!CS!: track 46.6 -> 0.00 mm, vias 3 -> 0
- net SD_DATA3: track 2.69 -> 43.7 mm, vias 1 -> 4
- net SD_!CS!: track 38.4 -> 24.8 mm
- net 3.3V_LP: track 24.1 -> 22.2 mm
- net SPI_SCK: track 4.69 -> 3.71 mm
- net SPI_CIPO: track 8.97 -> 8.01 mm
